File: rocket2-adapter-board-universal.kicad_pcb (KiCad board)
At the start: 2 copper layers, 45 x 55 mm, 15 parts, among them J2 Conn_01x04_Socket, J3 Conn_01x02_Socket, J4 Conn_01x04_Socket, J5 DSUB_15pin/VGA Veritical Fema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

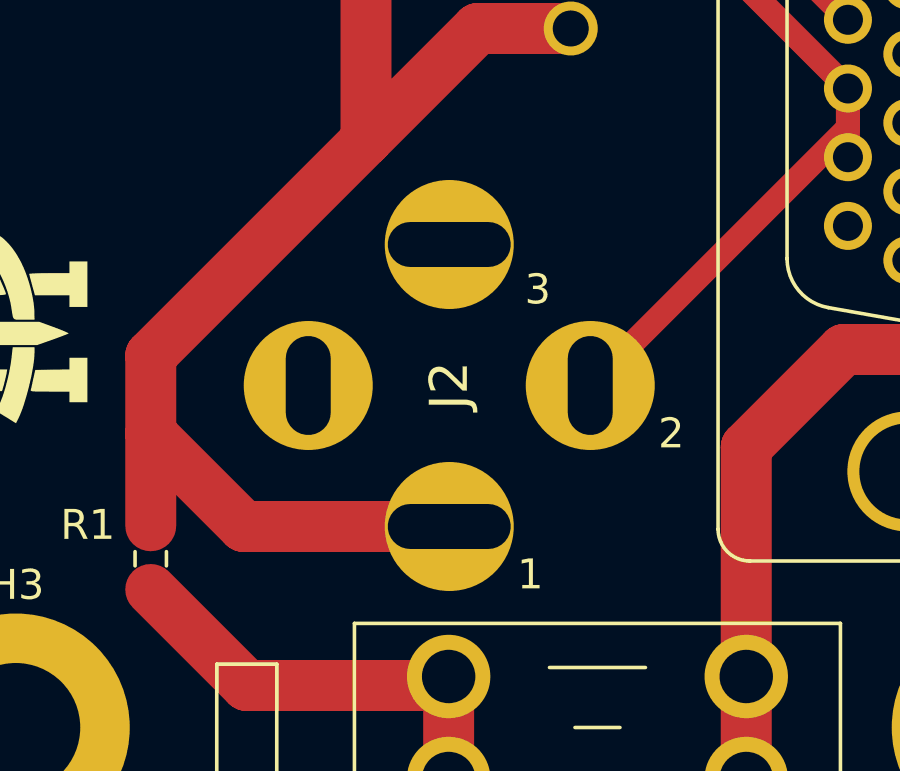
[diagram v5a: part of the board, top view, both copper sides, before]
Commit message: PT Footprint Update
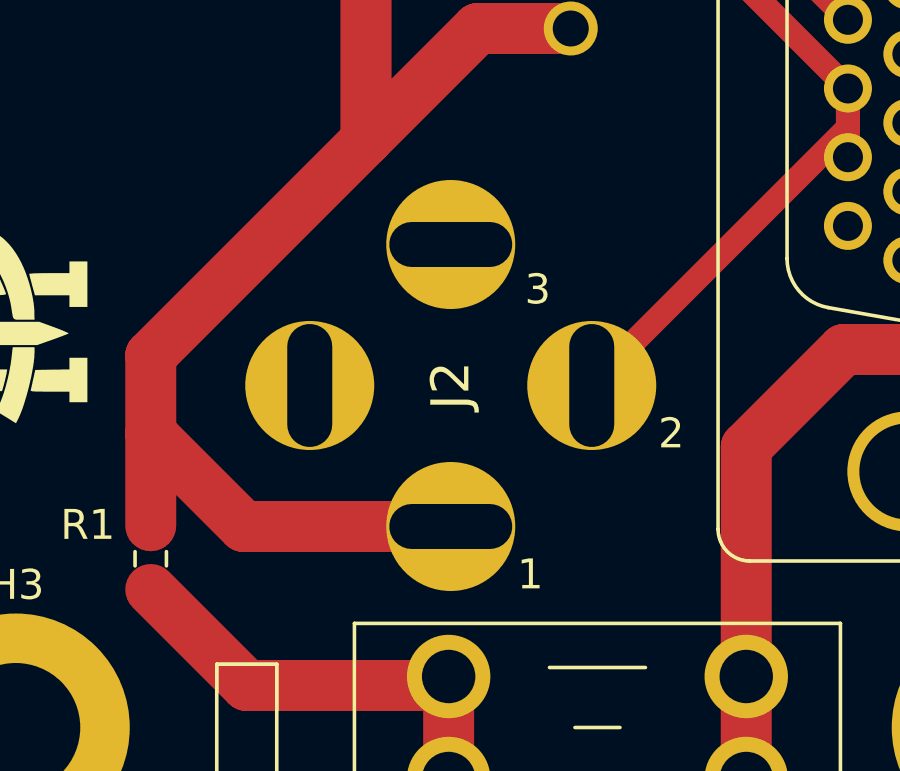
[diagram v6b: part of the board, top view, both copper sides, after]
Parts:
- moved J2 0.05 mm to (140.5, 97.6)
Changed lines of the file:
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@@
-		)
-	)
-	(footprint "UCIRP-KiCAD-Lib:Pad_Socket 9.4mm_MiniDIN"
-		(layer "F.Cu")
-		(at 140.45 97.6 90)
-		(descr "5749230-1-1")
-		(tags "Connector")
-		(property "Reference" "J2"
-			(at 0 0 90)
-			(layer "F.SilkS")
-			(effects
-				(font
-					(size 1.27 1.27)
-					(thickness 0.254)
-				)
-			)
-		)
-		(property "Value" "Conn_01x04_Socket"
-			(at -3.35 2.095 90)
-			(layer "F.SilkS")
-			(hide yes)
-			(effects
-				(font
-					(size 1.27 1.27)
-					(thickness 0.254)
-				)
-			)
-		)
-		(property "Datasheet" "~"
-			(at 0 0 90)
-			(layer "F.Fab")
-			(hide yes)
-			(effects
-				(font
-					(size 1.27 1.27)
-					(thickness 0.15)
-				)
-			)
-		)
-		(property "Description" "Generic connector, single row, 01x04, script generated"
-			(at 0 0 90)
-			(layer "F.Fab")
-			(hide yes)
-			(effects
-				(font
-					(size 1.27 1.27)
-					(thickness 0.15)
-				)
-			)
-		)
-		(property ki_fp_filters "Connector*:*_1x??_*")
-		(sheetname "/")
-		(sheetfile "rocket2-adapter-board-universal.kicad_sch")
-		(attr through_hole)
-		(fp_text user "${REFERENCE}"
-			(at -0.1 0.2 90)
-			(layer "F.Fab")
-			(effects
-				(font
-					(size 1.27 1.27)
-					(thickness 0.254)
-				)
-			)
-		)
-		(pad "1" thru_hole circle
-			(at -4.7 0 90)
-			(size 4.3 4.3)
-			(drill oval 1.5 4.1)
-			(layers "*.Cu" "*.Mask")
-			(remove_unused_layers no)
-			(net 5 "VBUS")
-			(pinfunction "Pin_1")
-			(pintype "passive")
-		)
-		(pad "2" thru_hole circle
-			(at 0 4.7 90)
-			(size 4.3 4.3)
-			(drill oval 3.3 1.5)
-			(layers "*.Cu" "*.Mask")
-			(remove_unused_layers no)
-			(net 3 "AIN+")
-			(pinfunction "Pin_2")
-			(pintype "passive")
-		)
-		(pad "3" thru_hole circle
-			(at 4.7 0 90)
-			(size 4.3 4.3)
-			(drill oval 1.5 4.1)
-			(layers "*.Cu" "*.Mask")
-			(remove_unused_layers no)
-			(net 2 "GND")
-			(pinfunction "Pin_3")
-			(pintype "passive")
-		)
-		(pad "4" thru_hole circle
-			(at 0 -4.7 90)
-			(size 4.3 4.3)
-			(drill oval 3.3 1.5)
-			(layers "*.Cu" "*.Mask")
-			(remove_unused_layers no)
-			(net 7 "unconnected-(J2-Pin_4-Pad4)")
-			(pinfunction "Pin_4")
-			(pintype "passive+no_connect")
-		)
-		(embedded_fonts no)
-		(model "5749230-1.stp"
-			(offset
-				(xyz -3.349999854 -8.510000101 6.689999957)
-			)
-			(scale
-				(xyz 1 1 1)
-			)
-			(rotate
-				(xyz -90 0 0)
-			)
 		)
 	)
@@
 			)
 		)
+	)
+	(footprint "UCIRP-KiCAD-Lib:Pad_Socket 9.4mm_MiniDIN"
+		(layer "F.Cu")
+		(at 140.5 97.6 90)
+		(descr "5749230-1-1")
+		(tags "Connector")
+		(property "Reference" "J2"
+			(at 0 0 90)
+			(layer "F.SilkS")
+			(effects
+				(font
+					(size 1.27 1.27)
+					(thickness 0.254)
+				)
+			)
+		)
+		(property "Value" "Conn_01x04_Socket"
+			(at -3.35 2.095 90)
+			(layer "F.SilkS")
+			(hide yes)
+			(effects
+				(font
+					(size 1.27 1.27)
+					(thickness 0.254)
+				)
+			)
+		)
+		(property "Datasheet" "~"
+			(at 0 0 90)
+			(layer "F.Fab")
+			(hide yes)
+			(effects
+				(font
+					(size 1.27 1.27)
+					(thickness 0.15)
+				)
+			)
+		)
+		(property "Description" "Generic connector, single row, 01x04, script generated"
+			(at 0 0 90)
+			(layer "F.Fab")
+			(hide yes)
+			(effects
+				(font
+					(size 1.27 1.27)
+					(thickness 0.15)
+				)
+			)
+		)
+		(property ki_fp_filters "Connector*:*_1x??_*")
+		(sheetname "/")
+		(sheetfile "rocket2-adapter-board-universal.kicad_sch")
+		(attr through_hole)
+		(fp_text user "${REFERENCE}"
+			(at -0.1 0.2 90)
+			(layer "F.Fab")
+			(effects
+				(font
+					(size 1.27 1.27)
+					(thickness 0.254)
+				)
+			)
+		)
+		(pad "1" thru_hole circle
+			(at -4.7 0 90)
+			(size 4.3 4.3)
+			(drill oval 1.5 4.1)
+			(layers "*.Cu" "*.Mask")
+			(remove_unused_layers no)
+			(net 5 "VBUS")
+			(pinfunction "Pin_1")
+			(pintype "passive")
+		)
+		(pad "2" thru_hole circle
+			(at 0 4.7 90)
+			(size 4.3 4.3)
+			(drill oval 4.1 1.5)
+			(layers "*.Cu" "*.Mask")
+			(remove_unused_layers no)
+			(net 3 "AIN+")
+			(pinfunction "Pin_2")
+			(pintype "passive")
+		)
+		(pad "3" thru_hole circle
+			(at 4.7 0 90)
+			(size 4.3 4.3)
+			(drill oval 1.5 4.1)
+			(layers "*.Cu" "*.Mask")
+			(remove_unused_layers no)
+			(net 2 "GND")
+			(pinfunction "Pin_3")
+			(pintype "passive")
+		)
+		(pad "4" thru_hole circle
+			(at 0 -4.7 90)
+			(size 4.3 4.3)
+			(drill oval 4.1 1.5)
+			(layers "*.Cu" "*.Mask")
+			(remove_unused_layers no)
+			(net 7 "unconnected-(J2-Pin_4-Pad4)")
+			(pinfunction "Pin_4")
+			(pintype "passive+no_connect")
+		)
+		(embedded_fonts no)
+		(model "5749230-1.stp"
+			(offset
+				(xyz -3.349999854 -8.510000101 6.689999957)
+			)
+			(scale
+				(xyz 1 1 1)
+			)
+			(rotate
+				(xyz -90 0 0)
+			)
+		)

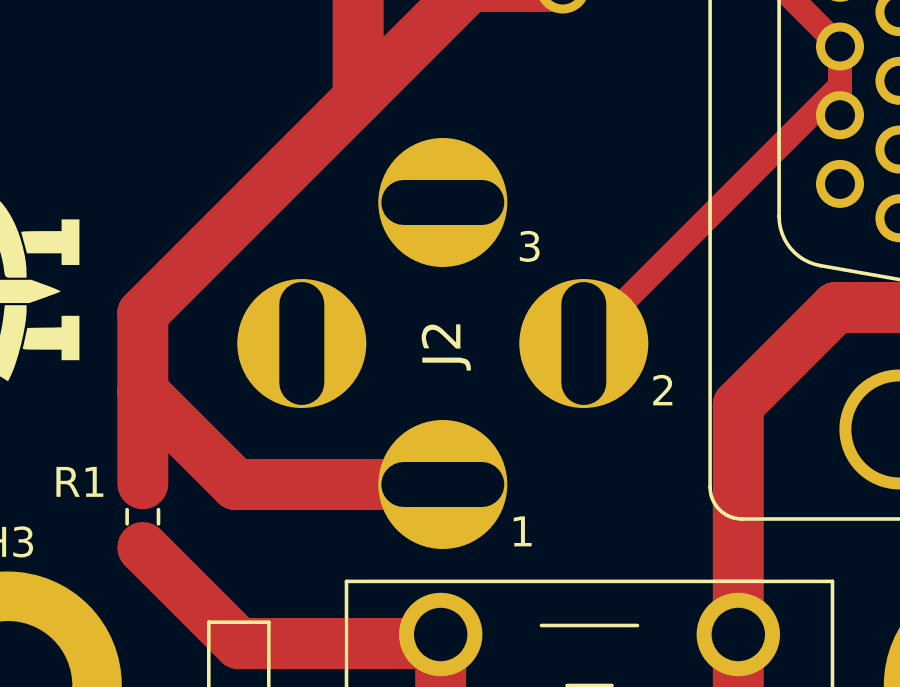
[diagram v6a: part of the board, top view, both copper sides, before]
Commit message: PT Footprint Update 2
Adjusted thickness to 1mm
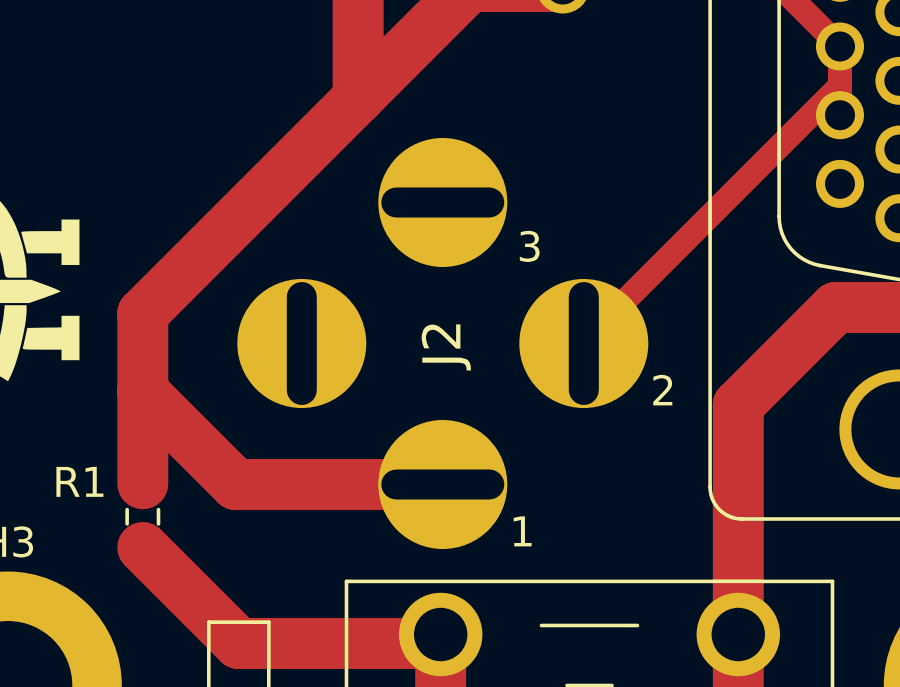
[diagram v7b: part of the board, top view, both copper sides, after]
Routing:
- net AIN+: track 47.7 -> 46.7 mm
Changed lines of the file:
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@@
 	(net 9 "unconnected-(J5-Pad11)")
 	(net 10 "unconnected-(J5-Pad0)_1")
+	(footprint "UCIRP-KiCAD-Lib:Pad_Socket 9.4mm_MiniDIN"
+		(layer "F.Cu")
+		(at 140.5 97.6 90)
+		(descr "5749230-1-1")
+		(tags "Connector")
+		(property "Reference" "J2"
+			(at 0 0 90)
+			(layer "F.SilkS")
+			(effects
+				(font
+					(size 1.27 1.27)
+					(thickness 0.254)
+				)
+			)
+		)
+		(property "Value" "Conn_01x04_Socket"
+			(at -3.35 2.095 90)
+			(layer "F.SilkS")
+			(hide yes)
+			(effects
+				(font
+					(size 1.27 1.27)
+					(thickness 0.254)
+				)
+			)
+		)
+		(property "Datasheet" "~"
+			(at 0 0 90)
+			(layer "F.Fab")
+			(hide yes)
+			(effects
+				(font
+					(size 1.27 1.27)
+					(thickness 0.15)
+				)
+			)
+		)
+		(property "Description" "Generic connector, single row, 01x04, script generated"
+			(at 0 0 90)
+			(layer "F.Fab")
+			(hide yes)
+			(effects
+				(font
+					(size 1.27 1.27)
+					(thickness 0.15)
+				)
+			)
+		)
+		(property ki_fp_filters "Connector*:*_1x??_*")
+		(sheetname "/")
+		(sheetfile "rocket2-adapter-board-universal.kicad_sch")
+		(attr through_hole)
+		(fp_text user "${REFERENCE}"
+			(at -0.1 0.2 90)
+			(layer "F.Fab")
+			(effects
+				(font
+					(size 1.27 1.27)
+					(thickness 0.254)
+				)
+			)
+		)
+		(pad "1" thru_hole circle
+			(at -4.7 0 90)
+			(size 4.3 4.3)
+			(drill oval 1 4.1)
+			(layers "*.Cu" "*.Mask")
+			(remove_unused_layers no)
+			(net 5 "VBUS")
+			(pinfunction "Pin_1")
+			(pintype "passive")
+		)
+		(pad "2" thru_hole circle
+			(at 0 4.7 90)
+			(size 4.3 4.3)
+			(drill oval 4.1 1)
+			(layers "*.Cu" "*.Mask")
+			(remove_unused_layers no)
+			(net 3 "AIN+")
+			(pinfunction "Pin_2")
+			(pintype "passive")
+		)
+		(pad "3" thru_hole circle
+			(at 4.7 0 90)
+			(size 4.3 4.3)
+			(drill oval 1 4.1)
+			(layers "*.Cu" "*.Mask")
+			(remove_unused_layers no)
+			(net 2 "GND")
+			(pinfunction "Pin_3")
+			(pintype "passive")
+		)
+		(pad "4" thru_hole circle
+			(at 0 -4.7 90)
+			(size 4.3 4.3)
+			(drill oval 4.1 1)
+			(layers "*.Cu" "*.Mask")
+			(remove_unused_layers no)
+			(net 7 "unconnected-(J2-Pin_4-Pad4)")
+			(pinfunction "Pin_4")
+			(pintype "passive+no_connect")
+		)
+		(embedded_fonts no)
+		(model "5749230-1.stp"
+			(offset
+				(xyz -3.349999854 -8.510000101 6.689999957)
+			)
+			(scale
+				(xyz 1 1 1)
+			)
+			(rotate
+				(xyz -90 0 0)
+			)
+		)
+	)
 	(footprint "UCIRP-KiCAD-Lib:Connector_VGA_Vertical"
 		(layer "F.Cu")
@@
 		)
 	)
-	(footprint "UCIRP-KiCAD-Lib:Pad_Socket 9.4mm_MiniDIN"
-		(layer "F.Cu")
-		(at 140.5 97.6 90)
-		(descr "5749230-1-1")
-		(tags "Connector")
-		(property "Reference" "J2"
-			(at 0 0 90)
-			(layer "F.SilkS")
-			(effects
-				(font
-					(size 1.27 1.27)
-					(thickness 0.254)
-				)
-			)
-		)
-		(property "Value" "Conn_01x04_Socket"
-			(at -3.35 2.095 90)
-			(layer "F.SilkS")
-			(hide yes)
-			(effects
-				(font
-					(size 1.27 1.27)
-					(thickness 0.254)
-				)
-			)
-		)
-		(property "Datasheet" "~"
-			(at 0 0 90)
-			(layer "F.Fab")
-			(hide yes)
-			(effects
-				(font
-					(size 1.27 1.27)
-					(thickness 0.15)
-				)
-			)
-		)
-		(property "Description" "Generic connector, single row, 01x04, script generated"
-			(at 0 0 90)
-			(layer "F.Fab")
-			(hide yes)
-			(effects
-				(font
-					(size 1.27 1.27)
-					(thickness 0.15)
-				)
-			)
-		)
-		(property ki_fp_filters "Connector*:*_1x??_*")
-		(sheetname "/")
-		(sheetfile "rocket2-adapter-board-universal.kicad_sch")
-		(attr through_hole)
-		(fp_text user "${REFERENCE}"
-			(at -0.1 0.2 90)
-			(layer "F.Fab")
-			(effects
-				(font
-					(size 1.27 1.27)
-					(thickness 0.254)
-				)
-			)
-		)
-		(pad "1" thru_hole circle
-			(at -4.7 0 90)
-			(size 4.3 4.3)
-			(drill oval 1.5 4.1)
-			(layers "*.Cu" "*.Mask")
-			(remove_unused_layers no)
-			(net 5 "VBUS")
-			(pinfunction "Pin_1")
-			(pintype "passive")
-		)
-		(pad "2" thru_hole circle
-			(at 0 4.7 90)
-			(size 4.3 4.3)
-			(drill oval 4.1 1.5)
-			(layers "*.Cu" "*.Mask")
-			(remove_unused_layers no)
-			(net 3 "AIN+")
-			(pinfunction "Pin_2")
-			(pintype "passive")
-		)
-		(pad "3" thru_hole circle
-			(at 4.7 0 90)
-			(size 4.3 4.3)
-			(drill oval 1.5 4.1)
-			(layers "*.Cu" "*.Mask")
-			(remove_unused_layers no)
-			(net 2 "GND")
-			(pinfunction "Pin_3")
-			(pintype "passive")
-		)
-		(pad "4" thru_hole circle
-			(at 0 -4.7 90)
-			(size 4.3 4.3)
-			(drill oval 4.1 1.5)
-			(layers "*.Cu" "*.Mask")
-			(remove_unused_layers no)
-			(net 7 "unconnected-(J2-Pin_4-Pad4)")
-			(pinfunction "Pin_4")
-			(pintype "passive+no_connect")
-		)
-		(embedded_fonts no)
-		(model "5749230-1.stp"
-			(offset
-				(xyz -3.349999854 -8.510000101 6.689999957)
-			)
-			(scale
-				(xyz 1 1 1)
-			)
-			(rotate
-				(xyz -90 0 0)
-			)
-		)
-	)
 	(footprint "MountingHole:MountingHole_4.3mm_M4_ISO7380_Pad"
 		(layer "F.Cu")
@@
 		(net 3)
 	)
-	(segment
-		(start 146.13 97.6)
-		(end 145.15 97.6)
-		(width 0.6)
-		(layer "B.Cu")
-		(net 3)
-	)
